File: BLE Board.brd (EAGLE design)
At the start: 52.3 x 67 mm, 39 parts, among them IC1 TM4C123GH6PM, IC2 TPS6300

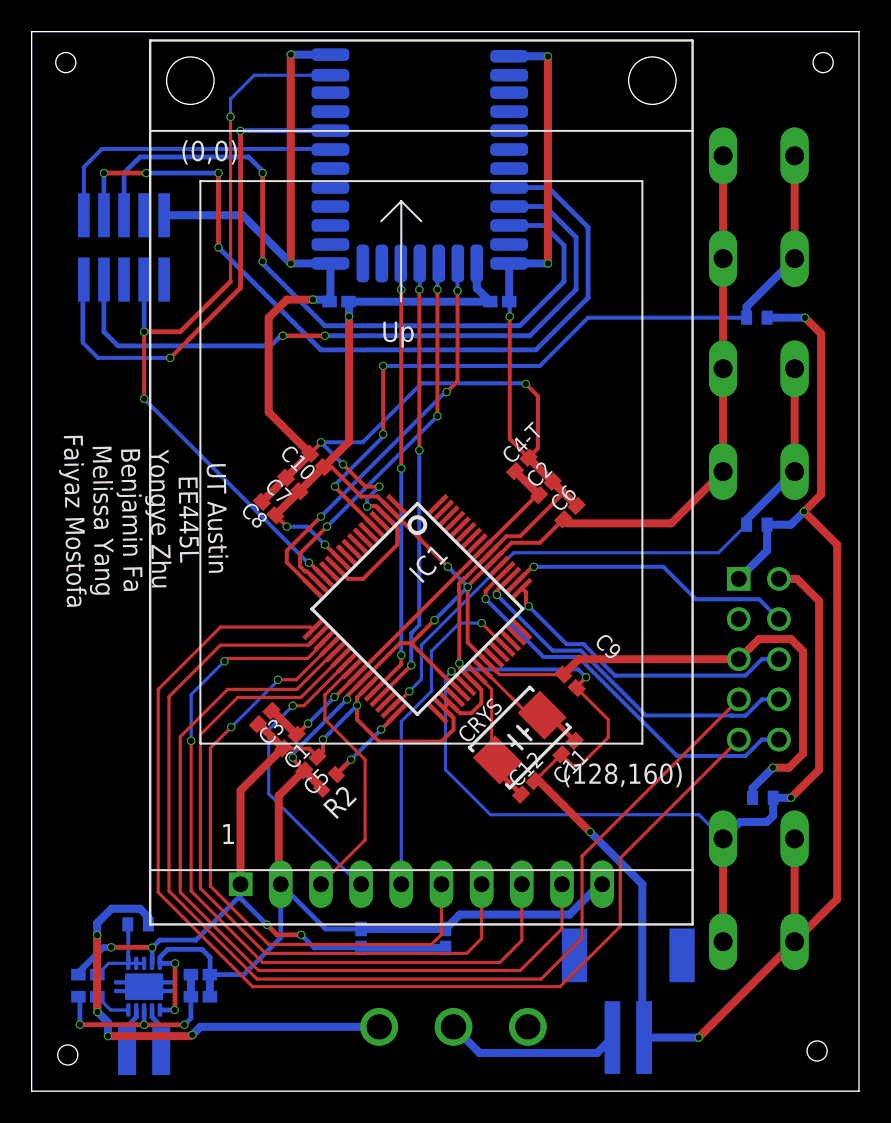
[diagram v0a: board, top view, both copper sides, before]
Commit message: 0603 cap/res, add test pts for gnd/pwr
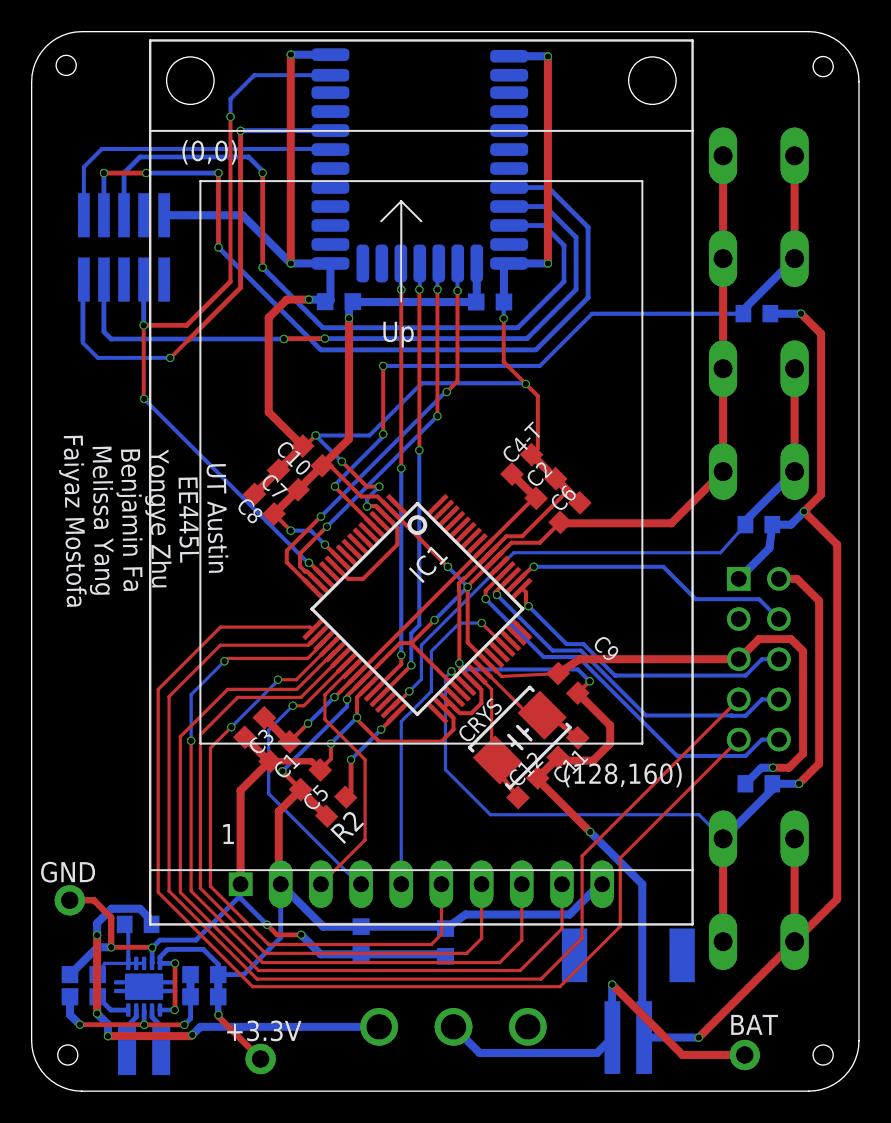
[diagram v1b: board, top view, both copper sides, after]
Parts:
- added +3.3V, BAT, GND: TP_KEYSTONE500X, EE445L:P1.1MM
- C1, C10, C11, C12, C13, C14, C15, C16, C17, C18-T, C19, C2, C20-T, C3, C4-T, C5, C6, C7, C8, C9: device EE445L:C0402K -> EE445L:C0603K
- R1, R2, R3, R4, R5: device EE445L:R0402 -> EE445L:R0603
- moved R2 1.64 mm to (12.6, 18.0)
- moved C5 1.02 mm to (11.0, 19.7)
- moved R1 0.92 mm to (39.4, 19.4)
- moved C3 0.90 mm to (7.49, 23.0)
- moved C1 0.90 mm to (9.09, 21.5)
- moved C18-T 0.61 mm to (22.4, 49.9)
- moved C7 0.40 mm to (9.63, 38.6)
- moved C10 0.40 mm to (11.2, 40.2)
- moved C8 0.40 mm to (8.10, 37.1)
- moved C15 0.25 mm to (-3.30, 7.37)
- moved C16 0.25 mm to (-3.30, 5.97)
- moved C13 0.25 mm to (4.32, 7.37)
- moved C14 0.25 mm to (4.32, 5.97)
- moved C19 0.25 mm to (19.6, 9.40)
- moved R4 0.25 mm to (39.2, 49.1)
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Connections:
- net +3V3: now also +3.3V.TP
- net BAT: now also BAT.TP
- net GND: now also GND.TP
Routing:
- net BAT: track 11.1 -> 24.7 mm, vias 0 -> 1
- net +3V3: track 196.6 -> 200.9 mm, vias 11 -> 12
- net WAKE: track 5.43 -> 6.62 mm
- net GND: track 307.5 -> 308.4 mm
- net RST: track 55.9 -> 55.2 mm
- net VDDC: track 26.0 -> 26.7 mm
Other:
- outline, holes or cut-outs redrawn

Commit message: Change direction of battery connector
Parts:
- moved B1 2.50 mm to (31.8, 4.67), turned to 180 degrees
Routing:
- net GND: track 308.4 -> 307.3 mm, vias 23 -> 22
- net BAT: track 24.7 -> 25.1 mm, vias 1 -> 0
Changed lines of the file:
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@@
 Melissa Yang
 Faiyaz Mostofa</text>
-<dimension x1="-3.429" y1="0" x2="42.525" y2="0" x3="19.548" y3="1.27" textsize="1.778" layer="1"/>
-<dimension x1="45.7" y1="3.175" x2="45.7" y2="63.805" x3="42.418" y3="33.49" textsize="1.778" layer="1"/>
 </plain>
 <attributes>
@@
 </autorouter>
 <elements>
-<element name="B1" library="microbuilder" package="JSTPH2" value="JST 2-PH" x="31.115" y="7.0866" smashed="yes" rot="MR0">
-<attribute name="NAME" x="33.3375" y="9.0551" size="0.8128" layer="26" ratio="18" rot="MR0"/>
-<attribute name="VALUE" x="33.3375" y="8.3566" size="0.4064" layer="28" ratio="10" rot="MR0"/>
+<element name="B1" library="microbuilder" package="JSTPH2" value="JST 2-PH" x="31.75" y="4.6736" smashed="yes" rot="MR180">
+<attribute name="NAME" x="29.5275" y="2.7051" size="0.8128" layer="26" ratio="18" rot="MR180"/>
+<attribute name="VALUE" x="29.5275" y="3.4036" size="0.4064" layer="28" ratio="10" rot="MR180"/>
 </element>
 <element name="C1" library="EE445L" package="C0603K" value="0.1uF" x="9.0932" y="21.463" smashed="yes" rot="R225">
@@
 <wire x1="19.558" y1="8.523" x2="19.431" y2="8.65" width="0.508" layer="16"/>
 <wire x1="19.431" y1="8.65" x2="14.224" y2="8.65" width="0.508" layer="16"/>
-<wire x1="41.6306" y1="9.4488" x2="35.5684" y2="3.3866" width="0.508" layer="1"/>
-<wire x1="35.5684" y1="3.3866" x2="32.115" y2="3.3866" width="0.508" layer="16"/>
 <wire x1="41.6306" y1="15.9512" x2="41.6306" y2="9.4488" width="0.508" layer="1"/>
-<wire x1="32.115" y1="3.3866" x2="32.004" y2="3.4976" width="0.508" layer="16"/>
 <wire x1="25.002715625" y1="40.242715625" x2="26.526715625" y2="38.718715625" width="0.508" layer="1"/>
 <wire x1="7.48388125" y1="37.728115625" x2="9.00788125" y2="39.252115625" width="0.508" layer="1"/>
@@
 <wire x1="21.828590625" y1="25.370746875" x2="21.209465625" y2="25.989871875" width="0.254" layer="1"/>
 <wire x1="6.604" y1="13.081" x2="6.604" y2="19.010925" width="0.508" layer="1"/>
-<wire x1="32.004" y1="13.081" x2="28.702" y2="16.383" width="0.508" layer="16"/>
-<wire x1="32.004" y1="3.4976" x2="32.004" y2="13.081" width="0.508" layer="16"/>
 <via x="28.702" y="16.383" extent="1-16" drill="0.381" diameter="0.55"/>
 <wire x1="28.702" y1="16.383" x2="25.4837375" y2="19.6012625" width="0.508" layer="1"/>
@@
 <via x="42.2275" y="36.6395" extent="1-16" drill="0.381" diameter="0.55"/>
 <via x="42.037" y="49.149" extent="1-16" drill="0.381" diameter="0.55"/>
-<via x="35.5684" y="3.3866" extent="1-16" drill="0.381" diameter="0.55"/>
 <wire x1="6.604" y1="19.010925" x2="8.43735625" y2="20.84428125" width="0.508" layer="1"/>
 <wire x1="8.43735625" y1="20.84428125" x2="8.47448125" y2="20.84428125" width="0.508" layer="1"/>
@@
 <wire x1="-1.5748" y1="10.9728" x2="-2.667" y2="12.065" width="0.4064" layer="1"/>
 <wire x1="-2.667" y1="12.065" x2="-4.191" y2="12.065" width="0.4064" layer="1"/>
+<wire x1="28.702" y1="16.383" x2="30.734" y2="14.351" width="0.4064" layer="16"/>
+<wire x1="30.734" y1="14.351" x2="30.734" y2="7.874" width="0.4064" layer="16"/>
+<wire x1="30.75" y1="8.3736" x2="31.75" y2="9.3736" width="0.4064" layer="16"/>
+<wire x1="31.75" y1="9.3736" x2="31.75" y2="11.557" width="0.4064" layer="16"/>
+<wire x1="31.75" y1="11.557" x2="32.766" y2="12.573" width="0.4064" layer="16"/>
+<wire x1="32.766" y1="12.573" x2="39.878" y2="12.573" width="0.4064" layer="16"/>
+<wire x1="39.878" y1="12.573" x2="41.6306" y2="10.8204" width="0.4064" layer="16"/>
+<wire x1="41.6306" y1="10.8204" x2="41.6306" y2="9.4488" width="0.4064" layer="16"/>
+<wire x1="30.734" y1="7.874" x2="30.75" y2="8.3736" width="0" layer="19" extent="16-16"/>
 </signal>
 <signal name="VDDC">
@@
 <contactref element="B1" pad="2"/>
 <contactref element="ON/OFF" pad="P$2"/>
-<wire x1="20.066" y1="4.064" x2="21.717" y2="2.413" width="0.508" layer="16"/>
-<wire x1="21.717" y1="2.413" x2="29.1414" y2="2.413" width="0.508" layer="16"/>
-<wire x1="29.1414" y1="2.413" x2="30.115" y2="3.3866" width="0.508" layer="16"/>
 <contactref element="BAT" pad="TP"/>
-<wire x1="38.481" y1="2.286" x2="34.544" y2="2.286" width="0.508" layer="1"/>
-<wire x1="34.544" y1="2.286" x2="30.099" y2="6.731" width="0.508" layer="1"/>
-<via x="30.099" y="6.731" extent="1-16" drill="0.381" diameter="0.55"/>
-<wire x1="30.099" y1="6.731" x2="30.099" y2="3.4026" width="0.508" layer="16"/>
-<wire x1="30.099" y1="3.4026" x2="30.115" y2="3.3866" width="0.508" layer="16"/>
+<wire x1="32.75" y1="8.3736" x2="34.7736" y2="6.35" width="0.4064" layer="16"/>
+<wire x1="34.7736" y1="6.35" x2="37.084" y2="6.35" width="0.4064" layer="16"/>
+<wire x1="38.481" y1="4.953" x2="38.481" y2="2.286" width="0.4064" layer="16"/>
+<wire x1="37.084" y1="6.35" x2="38.481" y2="4.953" width="0.4064" layer="16"/>
+<wire x1="31.39729375" y1="5.718" x2="31.372" y2="5.718" width="0.4064" layer="16"/>
+<wire x1="31.372" y1="5.718" x2="31.242" y2="5.588" width="0.4064" layer="16"/>
+<wire x1="32.75" y1="8.3736" x2="32.75" y2="7.07070625" width="0.4064" layer="16"/>
+<wire x1="32.75" y1="7.07070625" x2="31.39729375" y2="5.718" width="0.4064" layer="16"/>
+<wire x1="31.242" y1="5.588" x2="25.44195625" y2="5.588" width="0.4064" layer="16"/>
+<wire x1="25.44195625" y1="5.588" x2="25.41035625" y2="5.6196" width="0.4064" layer="16"/>
+<wire x1="25.41035625" y1="5.6196" x2="24.12164375" y2="5.6196" width="0.4064" layer="16"/>
+<wire x1="24.12164375" y1="5.6196" x2="24.09004375" y2="5.588" width="0.4064" layer="16"/>
+<wire x1="21.59" y1="5.588" x2="20.066" y2="4.064" width="0.4064" layer="16"/>
+<wire x1="24.09004375" y1="5.588" x2="21.59" y2="5.588" width="0.4064" layer="16"/>
 </signal>
 <signal name="IN">

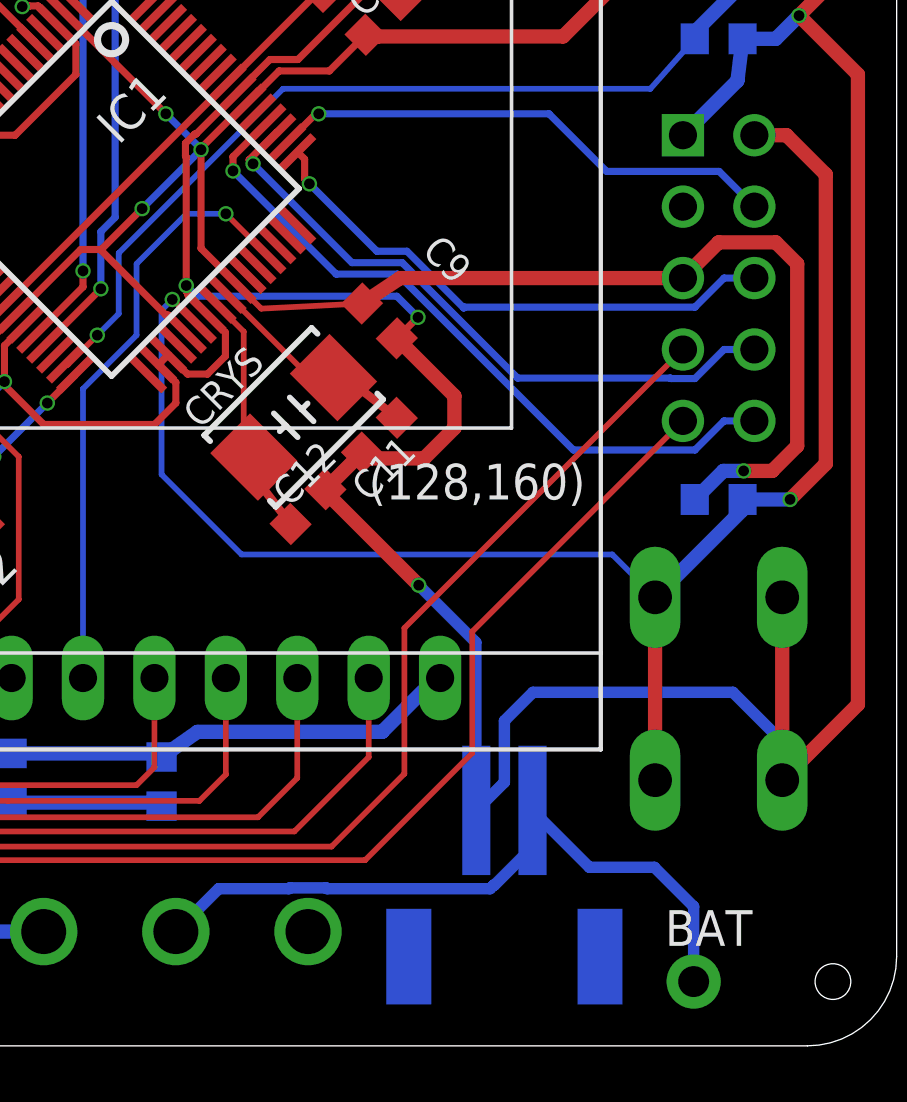
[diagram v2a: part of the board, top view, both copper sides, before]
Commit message: Fix wire issue
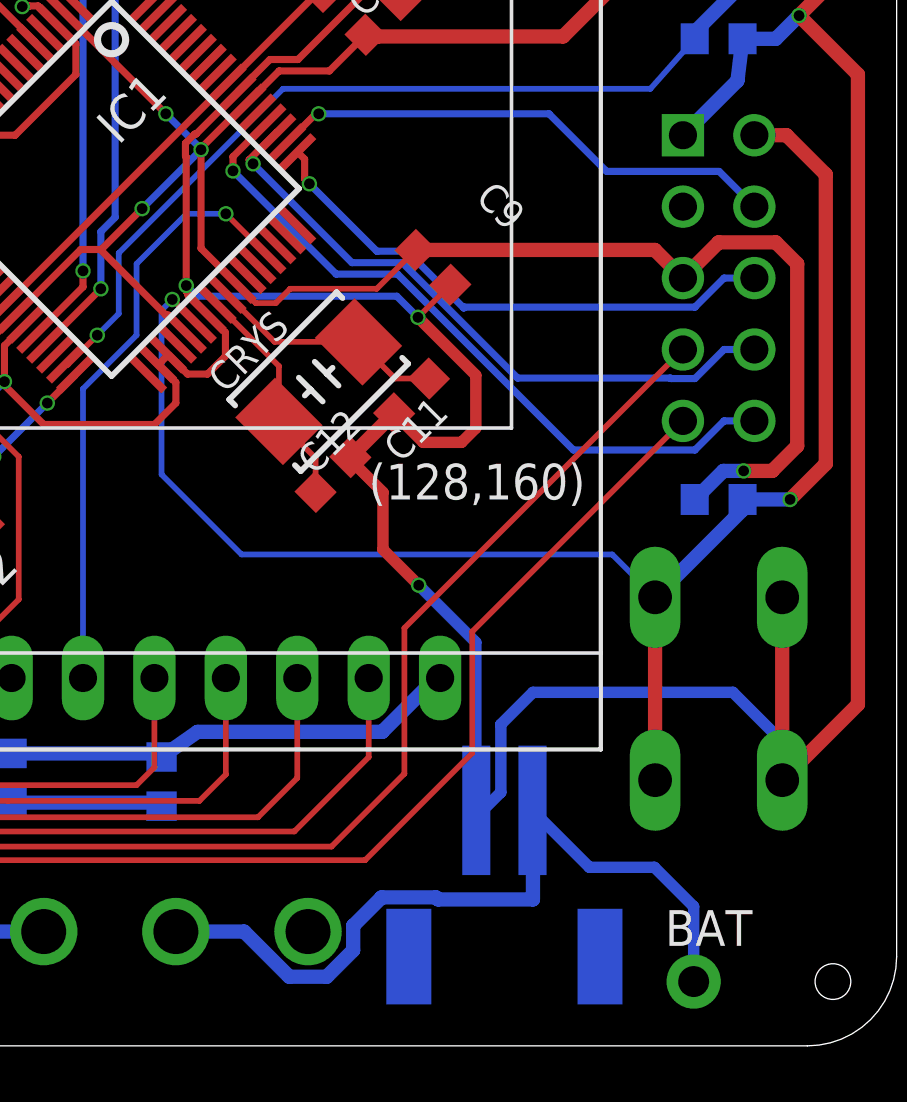
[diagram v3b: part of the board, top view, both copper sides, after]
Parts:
- moved C9 2.69 mm to (29.2, 27.7)
- moved C11 1.81 mm to (28.4, 23.1)
- moved CRYS 1.55 mm to (25.1, 23.6)
- moved C12 1.45 mm to (25.7, 20.3)
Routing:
- net BAT: track 25.1 -> 28.1 mm
- net GND: track 307.3 -> 310.1 mm
- net +3V3: track 200.9 -> 201.7 mm
- net OSC1: track 8.76 -> 8.08 mm
- net OSC0: track 7.72 -> 8.38 mm

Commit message: Final Commit
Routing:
- net BAT: track 28.1 -> 28.5 mm, vias 0 -> 1
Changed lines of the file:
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@@
 <drawing>
 <settings>
-<setting alwaysvectorfont="no"/>
+<setting alwaysvectorfont="yes"/>
 <setting verticaltext="up"/>
 </settings>
@@
 <contactref element="C11" pad="1"/>
 <contactref element="CRYS" pad="2"/>
-<wire x1="21.916571875" y1="26.696978125" x2="23.5773375" y2="25.0362125" width="0.2032" layer="1"/>
-<wire x1="23.5773375" y1="25.0362125" x2="26.5602125" y2="25.0362125" width="0.2032" layer="1"/>
-<wire x1="26.5602125" y1="25.0362125" x2="27.863709375" y2="23.732715625" width="0.2032" layer="1"/>
+<wire x1="26.5602125" y1="25.0362125" x2="26.6237125" y2="24.9727125" width="0.2032" layer="1"/>
+<wire x1="26.6237125" y1="24.9727125" x2="27.863709375" y2="23.732715625" width="0.2032" layer="1"/>
 <wire x1="27.863709375" y1="23.732715625" x2="29.066715625" y2="23.732715625" width="0.2032" layer="1"/>
+<wire x1="21.916571875" y1="26.696978125" x2="24.10255" y2="24.511" width="0.2032" layer="1"/>
+<wire x1="26.162" y1="24.511" x2="26.6237125" y2="24.9727125" width="0.2032" layer="1"/>
+<wire x1="24.10255" y1="24.511" x2="26.162" y2="24.511" width="0.2032" layer="1"/>
 </signal>
 <signal name="OSC1">
@@
 <wire x1="38.481" y1="4.953" x2="38.481" y2="2.286" width="0.4064" layer="16"/>
 <wire x1="37.084" y1="6.35" x2="38.481" y2="4.953" width="0.4064" layer="16"/>
-<wire x1="29.3183375" y1="5.28" x2="27.3816625" y2="5.28" width="0.508" layer="16"/>
-<wire x1="26.3724" y1="3.39860625" x2="25.43139375" y2="2.4576" width="0.508" layer="16"/>
-<wire x1="25.43139375" y1="2.4576" x2="24.10060625" y2="2.4576" width="0.508" layer="16"/>
-<wire x1="22.49420625" y1="4.064" x2="20.066" y2="4.064" width="0.508" layer="16"/>
-<wire x1="24.10060625" y1="2.4576" x2="22.49420625" y2="4.064" width="0.508" layer="16"/>
-<wire x1="29.3913375" y1="5.207" x2="32.766" y2="5.207" width="0.508" layer="16"/>
-<wire x1="29.3913375" y1="5.207" x2="29.3183375" y2="5.28" width="0.508" layer="16"/>
-<wire x1="27.3816625" y1="5.28" x2="26.3724" y2="4.2707375" width="0.508" layer="16"/>
-<wire x1="26.3724" y1="4.2707375" x2="26.3724" y2="3.39860625" width="0.508" layer="16"/>
-<wire x1="32.766" y1="5.207" x2="32.766" y2="8.3576" width="0.508" layer="16"/>
-<wire x1="32.766" y1="8.3576" x2="32.75" y2="8.3736" width="0.508" layer="16"/>
+<wire x1="32.75" y1="8.3736" x2="32.75" y2="4.429" width="0.508" layer="16"/>
+<wire x1="32.75" y1="4.429" x2="31.75" y2="3.429" width="0.508" layer="16"/>
+<via x="31.75" y="3.429" extent="1-16" drill="0.381" diameter="0.55"/>
+<wire x1="31.75" y1="3.429" x2="30.226" y2="1.905" width="0.508" layer="1"/>
+<wire x1="30.226" y1="1.905" x2="21.971" y2="1.905" width="0.508" layer="1"/>
+<wire x1="21.971" y1="1.905" x2="20.066" y2="3.81" width="0.508" layer="1"/>
+<wire x1="20.066" y1="3.81" x2="20.066" y2="4.064" width="0.508" layer="1"/>
 </signal>
 <signal name="IN">
